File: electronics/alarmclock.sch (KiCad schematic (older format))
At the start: 14 parts, among them SW1 Reset, U1 STM32F030C6Tx, Y1 24MHz

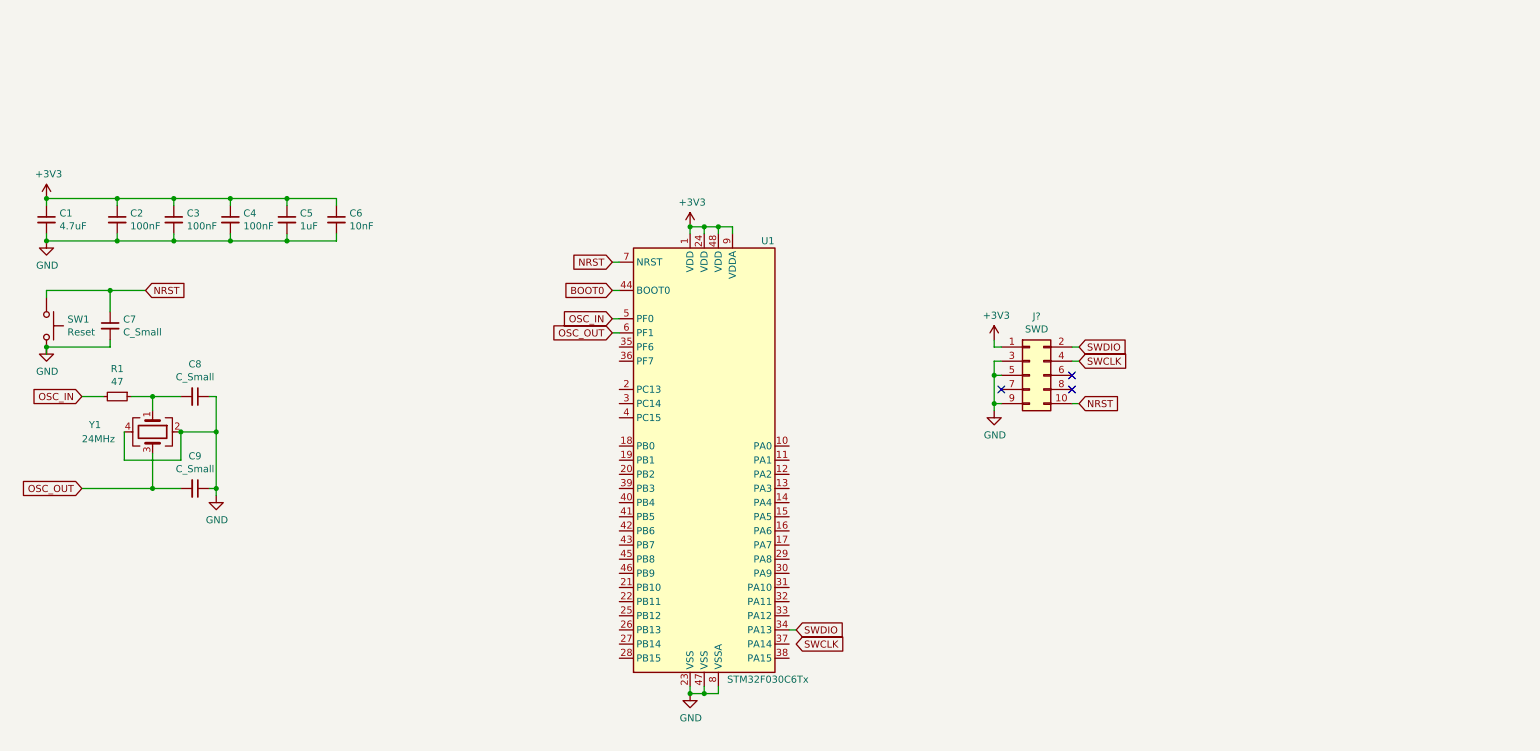
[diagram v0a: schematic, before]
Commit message: feat: CubeMX pinassignment and small schemetic changes
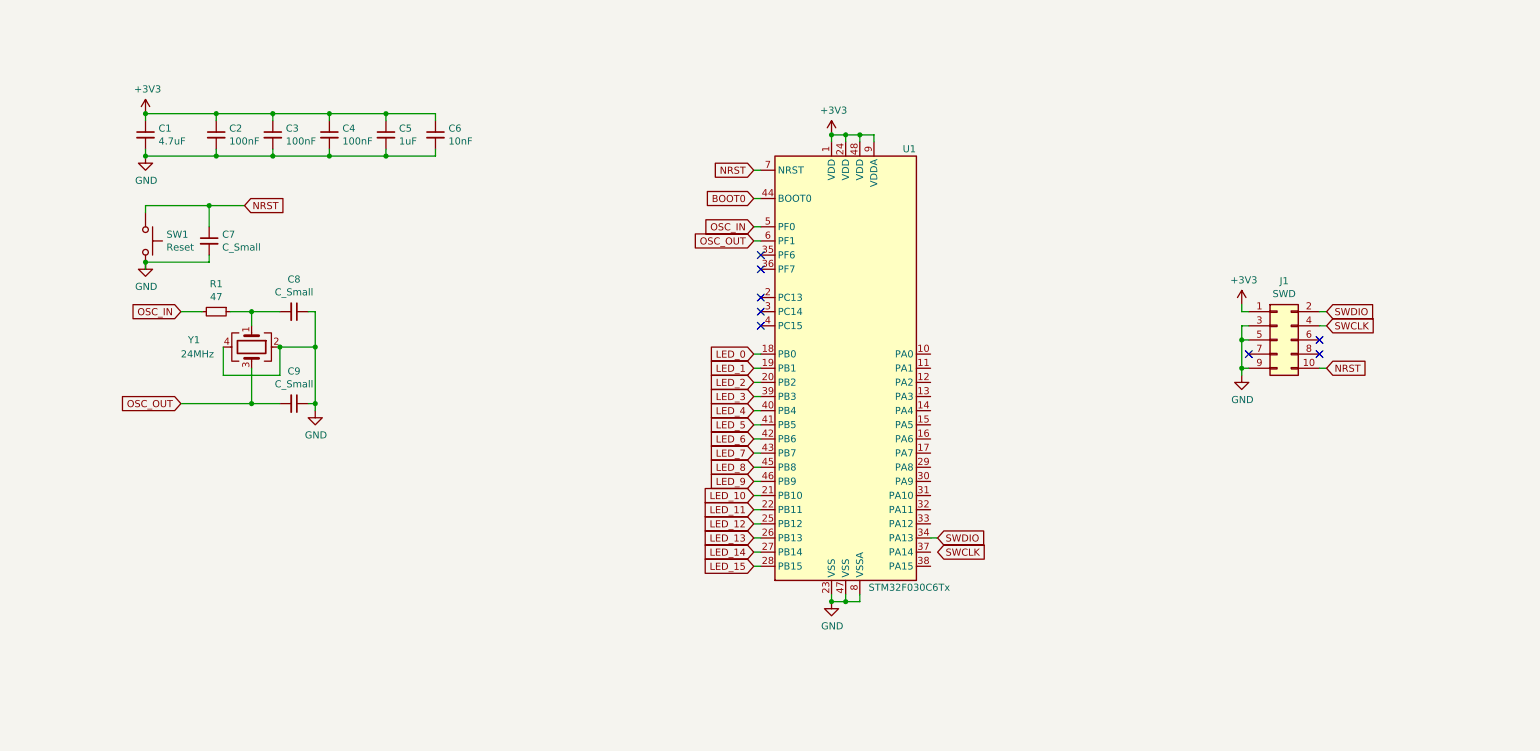
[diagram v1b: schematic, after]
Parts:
- gave numbers to parts that had none: 1
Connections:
- net LED_0: now reaches U1.18 (PB0)
- net LED_1: now reaches U1.19 (PB1)
- net LED_2: now reaches U1.20 (PB2)
- net LED_10: now reaches U1.21 (PB10)
- net LED_11: now reaches U1.22 (PB11)
- net LED_12: now reaches U1.25 (PB12)
- net LED_13: now reaches U1.26 (PB13)
- net LED_14: now reaches U1.27 (PB14)
- net LED_15: now reaches U1.28 (PB15)
- net LED_3: now reaches U1.39 (PB3)
- net LED_4: now reaches U1.40 (PB4)
- net LED_5: now reaches U1.41 (PB5)
- net LED_6: now reaches U1.42 (PB6)
- net LED_7: now reaches U1.43 (PB7)
- net LED_8: now reaches U1.45 (PB8)
- net LED_9: now reaches U1.46 (PB9)
- no-connect marks 3 -> 8
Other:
- moved on the sheet: C1, C2, C3, C4, C5, C6, C7, C8, C9, J1, R1, SW1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

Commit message: added headers for connecting the display, made first pcb layout
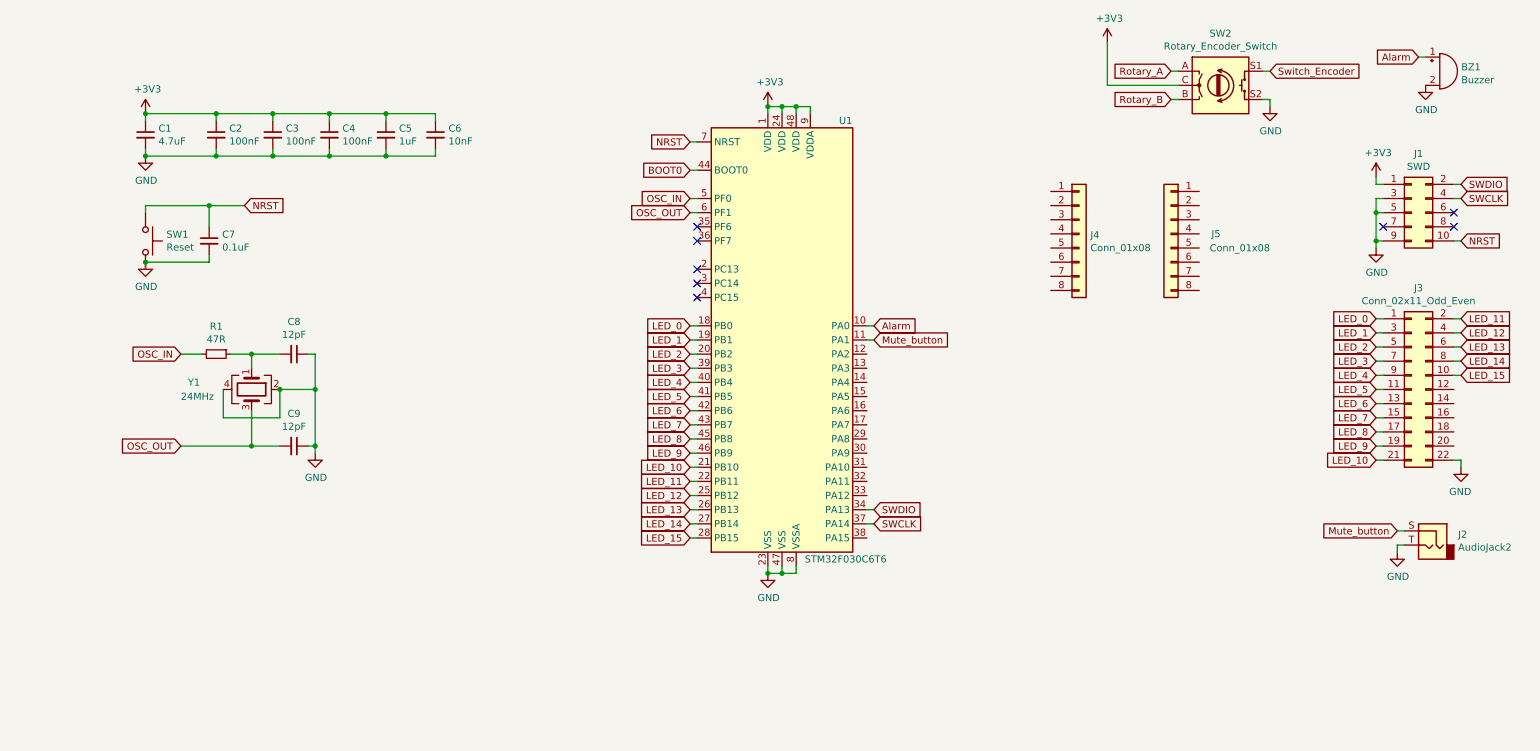
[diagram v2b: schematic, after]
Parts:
- added BZ1: Buzzer, symbol Device:Buzzer
- added J2: AudioJack2, Connector_Audio:Jack_3.5mm_CUI_SJ-3523-SMT_Horizontal, symbol Connector:AudioJack2
- added J3: Conn_02x11_Odd_Even, Connector_PinHeader_2.54mm:PinHeader_2x11_P2.54mm_Vertical, symbol Connector_Generic:Conn_02x11_Odd_Even
- added J4, J5: Conn_01x08, Connector_PinSocket_2.54mm:PinSocket_1x08_P2.54mm_Vertical, symbol Connector_Generic:Conn_01x08
- added SW2: Rotary_Encoder_Switch, symbol Device:Rotary_Encoder_Switch
- C1, C2, C3, C4, C5, C6: footprint (none) -> Capacitor_SMD:C_1206_3216Metric
- C7: value C_Small -> 0.1uF; footprint (none) -> Capacitor_SMD:C_1206_3216Metric
- C8, C9: value C_Small -> 12pF; footprint (none) -> Capacitor_SMD:C_1206_3216Metric
- J1: footprint (none) -> Connector_PinHeader_1.00mm:PinHeader_2x05_P1.00mm_Vertical
- R1: value 47 -> 47R; footprint (none) -> Resistor_SMD:R_1206_3216Metric
- SW1: footprint (none) -> Button_Switch_SMD:SW_DIP_SPSTx01_Slide_9.78x4.72mm_W8.61mm_P2.54mm
- U1: value STM32F030C6Tx -> STM32F030C6T6
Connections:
- net +3V3: now also SW2.C
- net GND: now also BZ1.2 (+), J2.T, J3.22 (Pin_22), SW2.S2
- net LED_0: now also J3.1 (Pin_1)
- net LED_1: now also J3.3 (Pin_3)
- net LED_10: now also J3.21 (Pin_21)
- net LED_11: now also J3.2 (Pin_2)
- net LED_12: now also J3.4 (Pin_4)
- net LED_13: now also J3.6 (Pin_6)
- net LED_14: now also J3.8 (Pin_8)
- net LED_15: now also J3.10 (Pin_10)
- net LED_2: now also J3.5 (Pin_5)
- net LED_3: now also J3.7 (Pin_7)
- net LED_4: now also J3.9 (Pin_9)
- net LED_5: now also J3.11 (Pin_11)
- net LED_6: now also J3.13 (Pin_13)
- net LED_7: now also J3.15 (Pin_15)
- net LED_8: now also J3.17 (Pin_17)
- net LED_9: now also J3.19 (Pin_19)
- net SWCLK: now also U1.37 (PA14)
- net Alarm: now reaches U1.10 (PA0)
- net Alarm: now also BZ1.1 (-)
- net Mute_button: now reaches U1.11 (PA1)
- net Mute_button: now also J2.S
- new net Rotary_A: SW2.A
- new net Rotary_B: SW2.B
- new net Switch_Encoder: SW2.S1
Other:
- moved on the sheet: C8, C9, J1, R1, U1, Y1

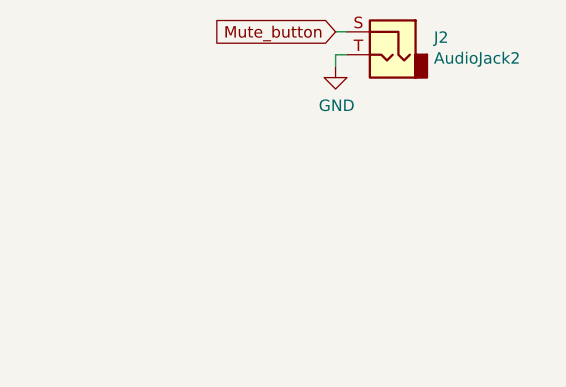
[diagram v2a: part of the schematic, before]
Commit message: refined pinout, changed solder pad sizes
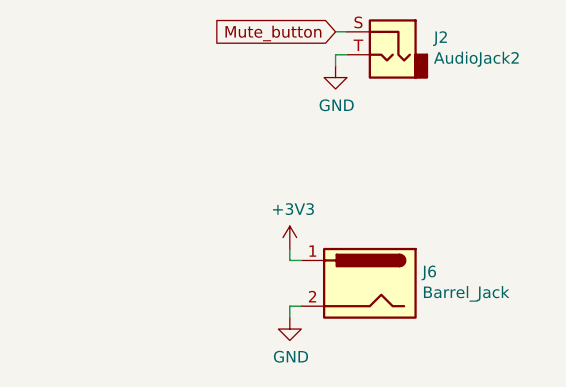
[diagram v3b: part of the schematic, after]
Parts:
- added J6: Barrel_Jack, Connector_PinHeader_1.00mm:PinHeader_1x02_P1.00mm_Vertical, symbol Connector:Barrel_Jack
- BZ1: footprint (none) -> Connector_PinHeader_1.00mm:PinHeader_1x02_P1.00mm_Vertical
- C2, C3, C4, C8, C9: footprint Capacitor_SMD:C_1206_3216Metric -> Capacitor_SMD:C_0201_0603Metric_Pad0.64x0.40mm_HandSolder
- C5: footprint Capacitor_SMD:C_1206_3216Metric -> Capacitor_SMD:C_0805_2012Metric_Pad1.18x1.45mm_HandSolder
- C6, C7: footprint Capacitor_SMD:C_1206_3216Metric -> Capacitor_SMD:C_0603_1608Metric_Pad1.08x0.95mm_HandSolder
- R1: footprint Resistor_SMD:R_1206_3216Metric -> Resistor_SMD:R_0201_0603Metric_Pad0.64x0.40mm_HandSolder
- Y1: footprint (none) -> Crystal:Crystal_SMD_0603-2Pin_6.0x3.5mm_HandSoldering
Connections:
- net +3V3: now also J6.1
- net GND: now also J6.2
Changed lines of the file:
@@
 F 0 "C7" H 1992 2196 50  0000 L CNN
 F 1 "0.1uF" H 1992 2105 50  0000 L CNN
-F 2 "Capacitor_SMD:C_1206_3216Metric" H 1900 2150 50  0001 C CNN
+F 2 "Capacitor_SMD:C_0603_1608Metric_Pad1.08x0.95mm_HandSolder" H 1900 2150 50  0001 C CNN
 F 3 "~" H 1900 2150 50  0001 C CNN
 	1    1900 2150
@@
 F 0 "R1" V 1754 2950 50  0000 C CNN
 F 1 "47R" V 1845 2950 50  0000 C CNN
-F 2 "Resistor_SMD:R_1206_3216Metric" H 1950 2950 50  0001 C CNN
+F 2 "Resistor_SMD:R_0201_0603Metric_Pad0.64x0.40mm_HandSolder" H 1950 2950 50  0001 C CNN
 F 3 "~" H 1950 2950 50  0001 C CNN
 	1    1950 2950
@@
 F 0 "C8" V 2271 2950 50  0000 C CNN
 F 1 "12pF" V 2362 2950 50  0000 C CNN
-F 2 "Capacitor_SMD:C_1206_3216Metric" H 2500 2950 50  0001 C CNN
+F 2 "Capacitor_SMD:C_0201_0603Metric_Pad0.64x0.40mm_HandSolder" H 2500 2950 50  0001 C CNN
 F 3 "~" H 2500 2950 50  0001 C CNN
 	1    2500 2950
@@
 F 0 "Y1" V 2150 2750 50  0000 L CNN
 F 1 "24MHz" V 2250 2700 50  0000 L CNN
-F 2 "" H 2200 3200 50  0001 C CNN
+F 2 "Crystal:Crystal_SMD_0603-2Pin_6.0x3.5mm_HandSoldering" H 2200 3200 50  0001 C CNN
 F 3 "~" H 2200 3200 50  0001 C CNN
 	1    2200 3200
@@
 F 0 "C9" V 2271 3600 50  0000 C CNN
 F 1 "12pF" V 2362 3600 50  0000 C CNN
-F 2 "Capacitor_SMD:C_1206_3216Metric" H 2500 3600 50  0001 C CNN
+F 2 "Capacitor_SMD:C_0201_0603Metric_Pad0.64x0.40mm_HandSolder" H 2500 3600 50  0001 C CNN
 F 3 "~" H 2500 3600 50  0001 C CNN
 	1    2500 3600
@@
 Wire Wire Line
 	10150 1700 10150 1750
-$Comp
-L power:+3V3 #PWR0106
-U 1 1 63CAFCBF
-P 10150 1700
-F 0 "#PWR0106" H 10150 1550 50  0001 C CNN
-F 1 "+3V3" H 10165 1873 50  0000 C CNN
-F 2 "" H 10150 1700 50  0001 C CNN
-F 3 "" H 10150 1700 50  0001 C CNN
-	1    10150 1700
-	1    0    0    -1
-$EndComp
 Wire Wire Line
 	5350 1950 5300 1950
@@
 F 0 "BZ1" H 10752 979 50  0000 L CNN
 F 1 "Buzzer" H 10752 888 50  0000 L CNN
-F 2 "" V 10575 1050 50  0001 C CNN
+F 2 "Connector_PinHeader_1.00mm:PinHeader_1x02_P1.00mm_Vertical" V 10575 1050 50  0001 C CNN
 F 3 "~" V 10575 1050 50  0001 C CNN
 	1    10600 950
@@
 F 0 "C2" H 2042 1446 50  0000 L CNN
 F 1 "100nF" H 2042 1355 50  0000 L CNN
-F 2 "Capacitor_SMD:C_1206_3216Metric" H 1950 1400 50  0001 C CNN
+F 2 "Capacitor_SMD:C_0201_0603Metric_Pad0.64x0.40mm_HandSolder" H 1950 1400 50  0001 C CNN
 F 3 "~" H 1950 1400 50  0001 C CNN
 	1    1950 1400
@@
 F 0 "C6" H 3592 1446 50  0000 L CNN
 F 1 "10nF" H 3592 1355 50  0000 L CNN
-F 2 "Capacitor_SMD:C_1206_3216Metric" H 3500 1400 50  0001 C CNN
+F 2 "Capacitor_SMD:C_0603_1608Metric_Pad1.08x0.95mm_HandSolder" H 3500 1400 50  0001 C CNN
 F 3 "~" H 3500 1400 50  0001 C CNN
 	1    3500 1400
@@
 F 0 "C5" H 3242 1446 50  0000 L CNN
 F 1 "1uF" H 3242 1355 50  0000 L CNN
-F 2 "Capacitor_SMD:C_1206_3216Metric" H 3150 1400 50  0001 C CNN
+F 2 "Capacitor_SMD:C_0805_2012Metric_Pad1.18x1.45mm_HandSolder" H 3150 1400 50  0001 C CNN
 F 3 "~" H 3150 1400 50  0001 C CNN
 	1    3150 1400
@@
 F 0 "C3" H 2442 1446 50  0000 L CNN
 F 1 "100nF" H 2442 1355 50  0000 L CNN
-F 2 "Capacitor_SMD:C_1206_3216Metric" H 2350 1400 50  0001 C CNN
+F 2 "Capacitor_SMD:C_0201_0603Metric_Pad0.64x0.40mm_HandSolder" H 2350 1400 50  0001 C CNN
 F 3 "~" H 2350 1400 50  0001 C CNN
 	1    2350 1400
@@
 F 0 "C4" H 2842 1446 50  0000 L CNN
 F 1 "100nF" H 2842 1355 50  0000 L CNN
-F 2 "Capacitor_SMD:C_1206_3216Metric" H 2750 1400 50  0001 C CNN
+F 2 "Capacitor_SMD:C_0201_0603Metric_Pad0.64x0.40mm_HandSolder" H 2750 1400 50  0001 C CNN
 F 3 "~" H 2750 1400 50  0001 C CNN
 	1    2750 1400
@@
 Wire Wire Line
 	6550 4150 6600 4150
+$Comp
+L Connector:Barrel_Jack J6
+U 1 1 63CA3C97
+P 10450 5300
+F 0 "J6" H 10220 5350 50  0000 R CNN
+F 1 "Barrel_Jack" H 10220 5259 50  0000 R CNN
+F 2 "Connector_PinHeader_1.00mm:PinHeader_1x02_P1.00mm_Vertical" H 10500 5260 50  0001 C CNN
+F 3 "~" H 10500 5260 50  0001 C CNN
+	1    10450 5300
+	-1   0    0    -1
+$EndComp
+$Comp
+L power:GND #PWR09
+U 1 1 63CB1D35
+P 10100 5450
+F 0 "#PWR09" H 10100 5200 50  0001 C CNN
+F 1 "GND" H 10105 5277 50  0000 C CNN
+F 2 "" H 10100 5450 50  0001 C CNN
+F 3 "" H 10100 5450 50  0001 C CNN
+	1    10100 5450
+	1    0    0    -1
+$EndComp
+Wire Wire Line
+	10100 5450 10100 5400
+Wire Wire Line
+	10100 5400 10150 5400
+$Comp
+L power:+3V3 #PWR0106
+U 1 1 63CAFCBF
+P 10150 1700
+F 0 "#PWR0106" H 10150 1550 50  0001 C CNN
+F 1 "+3V3" H 10165 1873 50  0000 C CNN
+F 2 "" H 10150 1700 50  0001 C CNN
+F 3 "" H 10150 1700 50  0001 C CNN
+	1    10150 1700
+	1    0    0    -1
+$EndComp
+$Comp
+L power:+3V3 #PWR08
+U 1 1 63CBC14B
+P 10100 5150
+F 0 "#PWR08" H 10100 5000 50  0001 C CNN
+F 1 "+3V3" H 10115 5323 50  0000 C CNN
+F 2 "" H 10100 5150 50  0001 C CNN
+F 3 "" H 10100 5150 50  0001 C CNN
+	1    10100 5150
+	1    0    0    -1
+$EndComp
+Wire Wire Line
+	10100 5150 10100 5200
+Wire Wire Line
+	10100 5200 10150 5200
 $EndSCHEMATC
